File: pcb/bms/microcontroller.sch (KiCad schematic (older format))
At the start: 16 parts, among them J18 SWD, SW3 SW_Push, SW4 SW_Push, U2 STM32L422KBTx

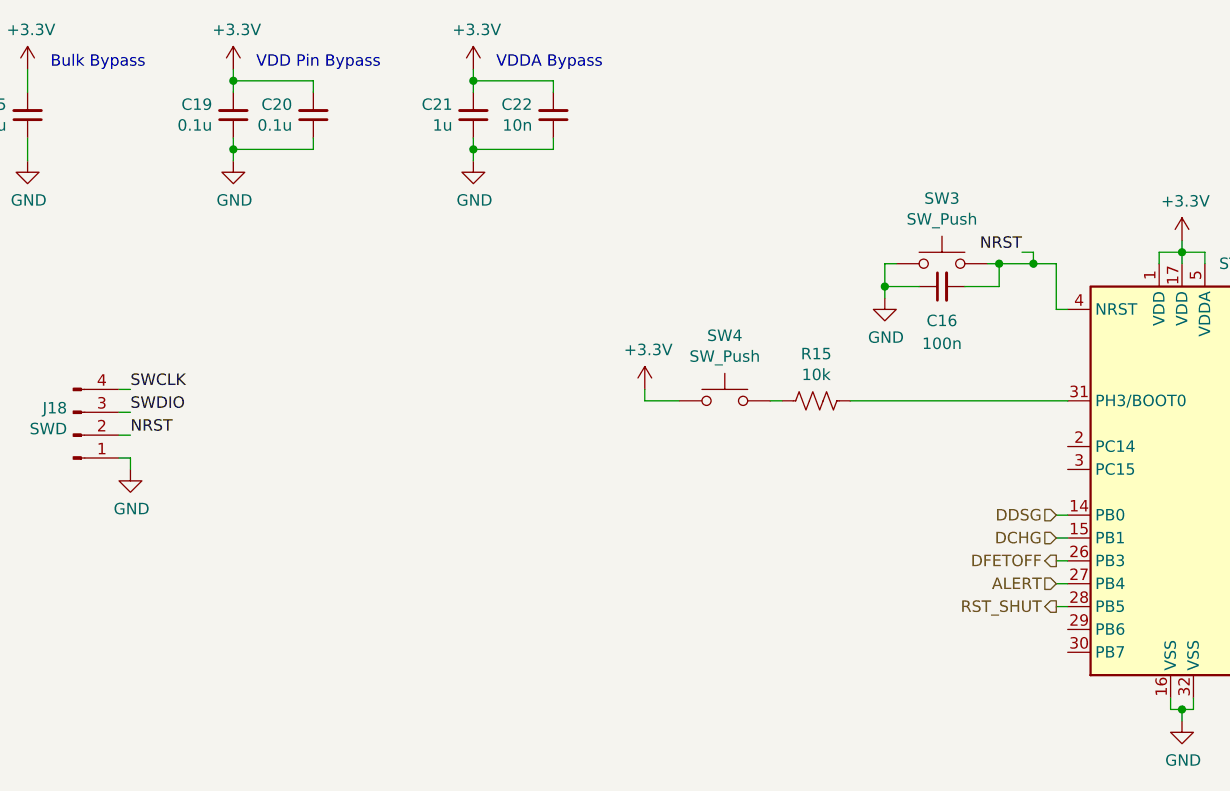
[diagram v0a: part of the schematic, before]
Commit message: split boards to two separate projects
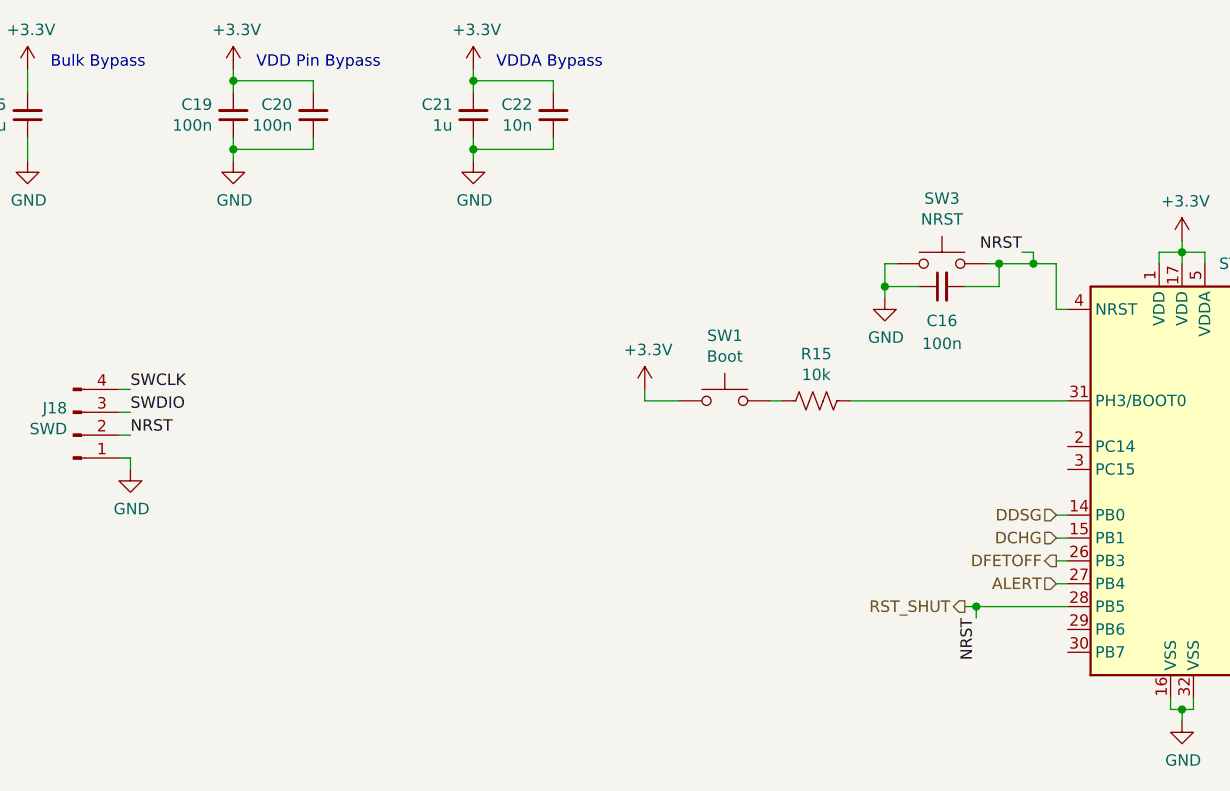
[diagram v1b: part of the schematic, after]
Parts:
- C19, C20: value 0.1u -> 100n
- J18: footprint (none) -> Connector_PinHeader_2.54mm:PinHeader_1x04_P2.54mm_Horizontal
- SW1: renamed from SW4; value SW_Push -> Boot; footprint (none) -> Buttons_Switches_SMD:SW_SPST_PTS645; MPN (none) -> PTS645SK50SMTR92 LFS; Manufacturer (none) -> C&K
- SW3: value SW_Push -> NRST; footprint (none) -> Buttons_Switches_SMD:SW_SPST_PTS645; MPN (none) -> PTS645SK50SMTR92 LFS; Manufacturer (none) -> C&K
- U2: MPN (none) -> STM32L422KBT6; Manufacturer (none) -> ST
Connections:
- net NRST is gone; now on net RST_SHUT: C16.2, J18.2 (Pin_2), SW3.2, U2.4 (NRST)
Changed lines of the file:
@@
 $Descr A4 11693 8268
 encoding utf-8
-Sheet 2 4
+Sheet 2 3
 Title ""
 Date ""
@@
 F 2 "Capacitor_SMD:C_0805_2012Metric" H 900 1050 50  0001 C CNN
 F 3 "~" H 900 1050 50  0001 C CNN
+F 4 "~" H 900 1050 50  0001 C CNN "MPN"
 	1    900  1050
 	1    0    0    1
@@
 F 2 "Package_QFP:LQFP-32_7x7mm_P0.8mm" H 5550 1700 50  0001 R CNN
 F 3 "http://www.st.com/st-web-ui/static/active/en/resource/technical/document/datasheet/DM00257195.pdf" H 5950 2600 50  0001 C CNN
+F 4 "STM32L422KBT6" H 5950 2600 50  0001 C CNN "MPN"
+F 5 "ST" H 5950 2600 50  0001 C CNN "Manufacturer"
 	1    5950 2600
 	1    0    0    -1
@@
 P 4900 1700
 F 0 "SW3" H 4900 1985 50  0000 C CNN
-F 1 "SW_Push" H 4900 1894 50  0000 C CNN
-F 2 "" H 4900 1900 50  0001 C CNN
+F 1 "NRST" H 4900 1894 50  0000 C CNN
+F 2 "Buttons_Switches_SMD:SW_SPST_PTS645" H 4900 1900 50  0001 C CNN
 F 3 "~" H 4900 1900 50  0001 C CNN
+F 4 "PTS645SK50SMTR92 LFS" H 4900 1700 50  0001 C CNN "MPN"
+F 5 "C&K" H 4900 1700 50  0001 C CNN "Manufacturer"
 	1    4900 1700
 	1    0    0    -1
 $EndComp
 $Comp
-L Switch:SW_Push SW4
+L Switch:SW_Push SW1
 U 1 1 609E9508
 P 3950 2300
-F 0 "SW4" H 3950 2585 50  0000 C CNN
-F 1 "SW_Push" H 3950 2494 50  0000 C CNN
-F 2 "" H 3950 2500 50  0001 C CNN
+F 0 "SW1" H 3950 2585 50  0000 C CNN
+F 1 "Boot" H 3950 2494 50  0000 C CNN
+F 2 "Buttons_Switches_SMD:SW_SPST_PTS645" H 3950 2500 50  0001 C CNN
 F 3 "~" H 3950 2500 50  0001 C CNN
+F 4 "PTS645SK50SMTR92 LFS" H 3950 2300 50  0001 C CNN "MPN"
+F 5 "C&K" H 3950 2300 50  0001 C CNN "Manufacturer"
 	1    3950 2300
 	1    0    0    -1
@@
 F 0 "J18" H 1073 2332 50  0000 R CNN
 F 1 "SWD" H 1073 2423 50  0000 R CNN
-F 2 "" H 1100 2450 50  0001 C CNN
+F 2 "Connector_PinHeader_2.54mm:PinHeader_1x04_P2.54mm_Horizontal" H 1100 2450 50  0001 C CNN
 F 3 "~" H 1100 2450 50  0001 C CNN
 	1    1100 2450
@@
 F 2 "Capacitor_SMD:C_0805_2012Metric" H 4900 1800 50  0001 C CNN
 F 3 "~" H 4900 1800 50  0001 C CNN
+F 4 "~" H 4900 1800 50  0001 C CNN "MPN"
 	1    4900 1800
 	0    -1   -1   0
@@
 F 2 "Capacitor_SMD:C_0805_2012Metric" H 2850 1050 50  0001 C CNN
 F 3 "~" H 2850 1050 50  0001 C CNN
+F 4 "~" H 2850 1050 50  0001 C CNN "MPN"
 	1    2850 1050
 	1    0    0    1
@@
 F 2 "Capacitor_SMD:C_0805_2012Metric" H 3200 1050 50  0001 C CNN
 F 3 "~" H 3200 1050 50  0001 C CNN
+F 4 "~" H 3200 1050 50  0001 C CNN "MPN"
 	1    3200 1050
 	1    0    0    1
@@
 P 2150 1050
 F 0 "C20" H 2058 1004 50  0000 R CNN
-F 1 "0.1u" H 2058 1095 50  0000 R CNN
+F 1 "100n" H 2058 1095 50  0000 R CNN
 F 2 "Capacitor_SMD:C_0805_2012Metric" H 2150 1050 50  0001 C CNN
 F 3 "~" H 2150 1050 50  0001 C CNN
+F 4 "~" H 2150 1050 50  0001 C CNN "MPN"
 	1    2150 1050
 	1    0    0    1
@@
 P 1800 1050
 F 0 "C19" H 1708 1004 50  0000 R CNN
-F 1 "0.1u" H 1708 1095 50  0000 R CNN
+F 1 "100n" H 1708 1095 50  0000 R CNN
 F 2 "Capacitor_SMD:C_0805_2012Metric" H 1800 1050 50  0001 C CNN
 F 3 "~" H 1800 1050 50  0001 C CNN
+F 4 "~" H 1800 1050 50  0001 C CNN "MPN"
 	1    1800 1050
 	1    0    0    1
 $EndComp
-Text HLabel 5400 3200 0    50   Output ~ 0
+Text HLabel 5000 3200 0    50   Output ~ 0
 RST_SHUT
-Wire Wire Line
-	5400 3200 5450 3200
+Text Label 5050 3250 3    50   ~ 0
+NRST
+Wire Wire Line
+	5000 3200 5050 3200
+Wire Wire Line
+	5050 3200 5050 3250
+Wire Wire Line
+	5050 3200 5450 3200
+Connection ~ 5050 3200
 $EndSCHEMATC

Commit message: pretty much ready to go
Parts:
- removed C16: 100n, Capacitor_SMD:C_0805_2012Metric, symbol Device:C_Small
- removed SW3: NRST, Buttons_Switches_SMD:SW_SPST_PTS645, symbol Switch:SW_Push
- added C27: 100n, Capacitor_SMD:C_0805_2012Metric, symbol Device:C_Small
- added C34, C36: 8p, Capacitor_SMD:C_0805_2012Metric, symbol Device:C_Small
- added D6, D7: 5.5V, Package_TO_SOT_SMD:SOT-23, symbol Device:D_TVS_x2_AAC
- added R37, R38: 20, Resistor_SMD:R_0805_2012Metric, symbol Device:R_US
- added R39: 10k, Resistor_SMD:R_0805_2012Metric, symbol Device:R_US
- added R42: Rext, Resistor_SMD:R_0805_2012Metric, symbol Device:R_US
- added X1: ASCO, Oscillator:Oscillator_SMD_Abracon_ASCO-4Pin_1.6x1.2mm, symbol Oscillator:ASCO
- added Y1: 32.768kHz, Crystal:Crystal_SMD_MicroCrystal_CC8V-T1A-2Pin_2.0x1.2mm_HandSoldering, symbol Device:Crystal
- C15: MPN (none) -> CL21A475KOCLRNC; Manufacturer (none) -> Samsung Electro-Mechanics
- C19, C20: MPN (none) -> CL21B104KCFSFNE; Manufacturer (none) -> Samsung Electro-Mechanics
- C21: MPN (none) -> CL21B105KBFNNNG; Manufacturer (none) -> Samsung Electro-Mechanics
- C22: MPN (none) -> CL21B103KBANNNC; Manufacturer (none) -> Samsung Electro-Mechanics
- J8: renamed from J18; MPN (none) -> PH1RB-04-UA; Manufacturer (none) -> Adam Tech
- R13, R14: value 22 -> 20; MPN (none) -> RMCF0805FT20R0; Manufacturer (none) -> Stackpole Electronics
- R15, R16, R17, R18: MPN (none) -> RMCF0805FT10K0; Manufacturer (none) -> Stackpole Electronics
- SW1: footprint Buttons_Switches_SMD:SW_SPST_PTS645 -> Button_Switch_SMD:SW_SPST_PTS645
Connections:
- net +3V3: now also C27.2, X1.1 (Tri-State), X1.4 (VDD)
- net DCHG: now also U2.14 (PB0); no longer U2.15 (PB1)
- net DDSG: now also U2.15 (PB1); no longer U2.14 (PB0)
- net GND: now also C27.1, C34.1, C36.1, D6.3 (common), D7.3 (common), R39.1, X1.2 (GND)
- net RST_SHUT: no longer J8.2 (Pin_2), U2.4 (NRST)
- net SWCLK: now also J8.3 (Pin_3); no longer J8.4 (Pin_4)
- net SWDIO: now also J8.4 (Pin_4); no longer J8.3 (Pin_3)
- net USART2_RX: now also D7.2 (A2), R38.1; no longer R17.2, U2.9 (PA3)
- net USART2_TX: now also D7.1 (A1), R37.1; no longer R16.2, U2.8 (PA2)
- net USB_DM: now also D6.2 (A2)
- net USB_DP: now also D6.1 (A1)
- net OSC_IN: now reaches U2.2 (PC14)
- net OSC_IN: now also C34.2, Y1.1
- net OSC_OUT: now reaches U2.3 (PC15)
- net OSC_OUT: now also R42.1
- net at R15.1, U2.31 (PH3/BOOT0): now also R39.2
- net HSE: now reaches U2.6 (PA0)
- net HSE: now also X1.3 (OUT)
- new net: C36.2, R42.2, Y1.2
- new net NRST: J8.2 (Pin_2), U2.4 (NRST)
- new net USART2_RX_: R17.2, R38.2, U2.9 (PA3)
- new net USART2_TX_: R16.2, R37.2, U2.8 (PA2)
- no-connect marks 0 -> 7
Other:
- moved on the sheet: R15, R17, R18, SW1
